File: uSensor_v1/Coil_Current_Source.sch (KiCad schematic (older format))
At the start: 12 parts

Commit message: Schematic in progress.
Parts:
- gave numbers to parts that had none: 12
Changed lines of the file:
@@
 P 5250 3700
 AR Path="/5C48099D" Ref="U?"  Part="1"
-AR Path="/5C398D6C/5C48099D" Ref="U?"  Part="1"
-AR Path="/5C839FF6/5C48099D" Ref="U?"  Part="1"
-F 0 "U?" H 5350 3800 50  0000 L CNN
+AR Path="/5C398D6C/5C48099D" Ref="U17"  Part="1"
+AR Path="/5C839FF6/5C48099D" Ref="U18"  Part="1"
+F 0 "U18" H 5350 3800 50  0000 L CNN
 F 1 "LM6132A/NS" H 5500 3800 50  0000 L CNN
 F 2 "" H 5250 3700 50  0001 C CNN
@@
 P 5500 3000
 AR Path="/5C4809A6" Ref="C?"  Part="1"
-AR Path="/5C398D6C/5C4809A6" Ref="C?"  Part="1"
-AR Path="/5C839FF6/5C4809A6" Ref="C?"  Part="1"
-F 0 "C?" H 5615 3046 50  0000 L CNN
+AR Path="/5C398D6C/5C4809A6" Ref="C54"  Part="1"
+AR Path="/5C839FF6/5C4809A6" Ref="C56"  Part="1"
+F 0 "C56" H 5615 3046 50  0000 L CNN
 F 1 "100n 6V3 X5R" H 5615 2955 50  0000 L CNN
 F 2 "Capacitor_SMD:C_0603_1608Metric_Pad1.05x0.95mm_HandSolder" H 5538 2850 50  0001 C CNN
@@
 P 5500 4600
 AR Path="/5C4809BF" Ref="C?"  Part="1"
-AR Path="/5C398D6C/5C4809BF" Ref="C?"  Part="1"
-AR Path="/5C839FF6/5C4809BF" Ref="C?"  Part="1"
-F 0 "C?" H 5615 4646 50  0000 L CNN
+AR Path="/5C398D6C/5C4809BF" Ref="C55"  Part="1"
+AR Path="/5C839FF6/5C4809BF" Ref="C57"  Part="1"
+F 0 "C57" H 5615 4646 50  0000 L CNN
 F 1 "100n 6V3 X5R" H 5615 4555 50  0000 L CNN
 F 2 "Capacitor_SMD:C_0603_1608Metric_Pad1.05x0.95mm_HandSolder" H 5538 4450 50  0001 C CNN
@@
 P 3900 4050
 AR Path="/5C4809DE" Ref="R?"  Part="1"
-AR Path="/5C398D6C/5C4809DE" Ref="R?"  Part="1"
-AR Path="/5C839FF6/5C4809DE" Ref="R?"  Part="1"
-F 0 "R?" H 3970 4096 50  0000 L CNN
+AR Path="/5C398D6C/5C4809DE" Ref="R42"  Part="1"
+AR Path="/5C839FF6/5C4809DE" Ref="R49"  Part="1"
+F 0 "R49" H 3970 4096 50  0000 L CNN
 F 1 "10k 1%" H 3970 4005 50  0000 L CNN
 F 2 "Resistor_SMD:R_0603_1608Metric_Pad1.05x0.95mm_HandSolder" V 3830 4050 50  0001 C CNN
@@
 P 3900 3550
 AR Path="/5C4809E6" Ref="R?"  Part="1"
-AR Path="/5C398D6C/5C4809E6" Ref="R?"  Part="1"
-AR Path="/5C839FF6/5C4809E6" Ref="R?"  Part="1"
-F 0 "R?" H 3970 3596 50  0000 L CNN
+AR Path="/5C398D6C/5C4809E6" Ref="R40"  Part="1"
+AR Path="/5C839FF6/5C4809E6" Ref="R47"  Part="1"
+F 0 "R47" H 3970 3596 50  0000 L CNN
 F 1 "10k 1%" H 3970 3505 50  0000 L CNN
 F 2 "Resistor_SMD:R_0603_1608Metric_Pad1.05x0.95mm_HandSolder" V 3830 3550 50  0001 C CNN
@@
 P 3450 3550
 AR Path="/5C4809ED" Ref="R?"  Part="1"
-AR Path="/5C398D6C/5C4809ED" Ref="R?"  Part="1"
-AR Path="/5C839FF6/5C4809ED" Ref="R?"  Part="1"
-F 0 "R?" H 3520 3596 50  0000 L CNN
+AR Path="/5C398D6C/5C4809ED" Ref="R39"  Part="1"
+AR Path="/5C839FF6/5C4809ED" Ref="R46"  Part="1"
+F 0 "R46" H 3520 3596 50  0000 L CNN
 F 1 "10k 1%" H 3520 3505 50  0000 L CNN
 F 2 "Resistor_SMD:R_0603_1608Metric_Pad1.05x0.95mm_HandSolder" V 3380 3550 50  0001 C CNN
@@
 P 6700 3400
 AR Path="/5C4809FD" Ref="Q?"  Part="1"
-AR Path="/5C398D6C/5C4809FD" Ref="Q?"  Part="1"
-AR Path="/5C839FF6/5C4809FD" Ref="Q?"  Part="1"
-F 0 "Q?" H 6891 3446 50  0000 L CNN
+AR Path="/5C398D6C/5C4809FD" Ref="Q3"  Part="1"
+AR Path="/5C839FF6/5C4809FD" Ref="Q5"  Part="1"
+F 0 "Q5" H 6891 3446 50  0000 L CNN
 F 1 "Q_NPN_BCE" H 6891 3355 50  0000 L CNN
 F 2 "" H 6900 3500 50  0001 C CNN
@@
 P 6700 4000
 AR Path="/5C480A04" Ref="Q?"  Part="1"
-AR Path="/5C398D6C/5C480A04" Ref="Q?"  Part="1"
-AR Path="/5C839FF6/5C480A04" Ref="Q?"  Part="1"
-F 0 "Q?" H 6891 3954 50  0000 L CNN
+AR Path="/5C398D6C/5C480A04" Ref="Q4"  Part="1"
+AR Path="/5C839FF6/5C480A04" Ref="Q6"  Part="1"
+F 0 "Q6" H 6891 3954 50  0000 L CNN
 F 1 "Q_PNP_BCE" H 6891 4045 50  0000 L CNN
 F 2 "" H 6900 4100 50  0001 C CNN
@@
 P 6550 3700
 AR Path="/5C480A0B" Ref="R?"  Part="1"
-AR Path="/5C398D6C/5C480A0B" Ref="R?"  Part="1"
-AR Path="/5C839FF6/5C480A0B" Ref="R?"  Part="1"
-F 0 "R?" V 6450 3700 50  0000 C CNN
+AR Path="/5C398D6C/5C480A0B" Ref="R41"  Part="1"
+AR Path="/5C839FF6/5C480A0B" Ref="R48"  Part="1"
+F 0 "R48" V 6450 3700 50  0000 C CNN
 F 1 "10k" V 6650 3700 50  0000 C CNN
 F 2 "Resistor_SMD:R_0603_1608Metric_Pad1.05x0.95mm_HandSolder" V 6480 3700 50  0001 C CNN
@@
 P 6800 2950
 AR Path="/5C480A1D" Ref="R?"  Part="1"
-AR Path="/5C398D6C/5C480A1D" Ref="R?"  Part="1"
-AR Path="/5C839FF6/5C480A1D" Ref="R?"  Part="1"
-F 0 "R?" H 6870 2996 50  0000 L CNN
+AR Path="/5C398D6C/5C480A1D" Ref="R38"  Part="1"
+AR Path="/5C839FF6/5C480A1D" Ref="R45"  Part="1"
+F 0 "R45" H 6870 2996 50  0000 L CNN
 F 1 "1R" H 6870 2905 50  0000 L CNN
 F 2 "Resistor_SMD:R_0603_1608Metric_Pad1.05x0.95mm_HandSolder" V 6730 2950 50  0001 C CNN
@@
 P 6800 4450
 AR Path="/5C480A25" Ref="R?"  Part="1"
-AR Path="/5C398D6C/5C480A25" Ref="R?"  Part="1"
-AR Path="/5C839FF6/5C480A25" Ref="R?"  Part="1"
-F 0 "R?" H 6870 4496 50  0000 L CNN
+AR Path="/5C398D6C/5C480A25" Ref="R44"  Part="1"
+AR Path="/5C839FF6/5C480A25" Ref="R51"  Part="1"
+F 0 "R51" H 6870 4496 50  0000 L CNN
 F 1 "1R" H 6870 4405 50  0000 L CNN
 F 2 "Resistor_SMD:R_0603_1608Metric_Pad1.05x0.95mm_HandSolder" V 6730 4450 50  0001 C CNN
@@
 P 8200 4250
 AR Path="/5C480A49" Ref="R?"  Part="1"
-AR Path="/5C398D6C/5C480A49" Ref="R?"  Part="1"
-AR Path="/5C839FF6/5C480A49" Ref="R?"  Part="1"
-F 0 "R?" V 8100 4250 50  0000 C CNN
+AR Path="/5C398D6C/5C480A49" Ref="R43"  Part="1"
+AR Path="/5C839FF6/5C480A49" Ref="R50"  Part="1"
+F 0 "R50" V 8100 4250 50  0000 C CNN
 F 1 "10R" V 8300 4250 50  0000 C CNN
 F 2 "Resistor_SMD:R_0603_1608Metric_Pad1.05x0.95mm_HandSolder" V 8130 4250 50  0001 C CNN

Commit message: Schematic in progress.
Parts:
- Q3, Q4: footprint (none) -> TBD
- U17: value LM6132A/NS -> TBD LM6132A/NS
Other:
- note added: "?"
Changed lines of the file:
@@
 $Descr A4 11693 8268
 encoding utf-8
-Sheet 4 7
+Sheet 3 7
 Title ""
 Date ""
@@
 AR Path="/5C398D6C/5C48099D" Ref="U17"  Part="1"
 AR Path="/5C839FF6/5C48099D" Ref="U18"  Part="1"
-F 0 "U18" H 5350 3800 50  0000 L CNN
-F 1 "LM6132A/NS" H 5500 3800 50  0000 L CNN
+F 0 "U17" H 5350 3800 50  0000 L CNN
+F 1 "TBD LM6132A/NS" H 5350 3550 50  0000 L CNN
 F 2 "" H 5250 3700 50  0001 C CNN
 F 3 "http://www.analog.com/media/en/technical-documentation/data-sheets/AD8603_8607_8609.pdf" H 5250 3900 50  0001 C CNN
@@
 AR Path="/5C398D6C/5C4809A6" Ref="C54"  Part="1"
 AR Path="/5C839FF6/5C4809A6" Ref="C56"  Part="1"
-F 0 "C56" H 5615 3046 50  0000 L CNN
+F 0 "C54" H 5615 3046 50  0000 L CNN
 F 1 "100n 6V3 X5R" H 5615 2955 50  0000 L CNN
 F 2 "Capacitor_SMD:C_0603_1608Metric_Pad1.05x0.95mm_HandSolder" H 5538 2850 50  0001 C CNN
@@
 AR Path="/5C398D6C/5C4809BF" Ref="C55"  Part="1"
 AR Path="/5C839FF6/5C4809BF" Ref="C57"  Part="1"
-F 0 "C57" H 5615 4646 50  0000 L CNN
+F 0 "C55" H 5615 4646 50  0000 L CNN
 F 1 "100n 6V3 X5R" H 5615 4555 50  0000 L CNN
 F 2 "Capacitor_SMD:C_0603_1608Metric_Pad1.05x0.95mm_HandSolder" H 5538 4450 50  0001 C CNN
@@
 AR Path="/5C398D6C/5C4809DE" Ref="R42"  Part="1"
 AR Path="/5C839FF6/5C4809DE" Ref="R49"  Part="1"
-F 0 "R49" H 3970 4096 50  0000 L CNN
+F 0 "R42" H 3970 4096 50  0000 L CNN
 F 1 "10k 1%" H 3970 4005 50  0000 L CNN
 F 2 "Resistor_SMD:R_0603_1608Metric_Pad1.05x0.95mm_HandSolder" V 3830 4050 50  0001 C CNN
@@
 AR Path="/5C398D6C/5C4809E6" Ref="R40"  Part="1"
 AR Path="/5C839FF6/5C4809E6" Ref="R47"  Part="1"
-F 0 "R47" H 3970 3596 50  0000 L CNN
+F 0 "R40" H 3970 3596 50  0000 L CNN
 F 1 "10k 1%" H 3970 3505 50  0000 L CNN
 F 2 "Resistor_SMD:R_0603_1608Metric_Pad1.05x0.95mm_HandSolder" V 3830 3550 50  0001 C CNN
@@
 AR Path="/5C398D6C/5C4809ED" Ref="R39"  Part="1"
 AR Path="/5C839FF6/5C4809ED" Ref="R46"  Part="1"
-F 0 "R46" H 3520 3596 50  0000 L CNN
+F 0 "R39" H 3520 3596 50  0000 L CNN
 F 1 "10k 1%" H 3520 3505 50  0000 L CNN
 F 2 "Resistor_SMD:R_0603_1608Metric_Pad1.05x0.95mm_HandSolder" V 3380 3550 50  0001 C CNN
@@
 AR Path="/5C398D6C/5C4809FD" Ref="Q3"  Part="1"
 AR Path="/5C839FF6/5C4809FD" Ref="Q5"  Part="1"
-F 0 "Q5" H 6891 3446 50  0000 L CNN
+F 0 "Q3" H 6891 3446 50  0000 L CNN
 F 1 "Q_NPN_BCE" H 6891 3355 50  0000 L CNN
-F 2 "" H 6900 3500 50  0001 C CNN
+F 2 "TBD" H 6900 3500 50  0001 C CNN
 F 3 "~" H 6700 3400 50  0001 C CNN
 	1    6700 3400
@@
 AR Path="/5C398D6C/5C480A04" Ref="Q4"  Part="1"
 AR Path="/5C839FF6/5C480A04" Ref="Q6"  Part="1"
-F 0 "Q6" H 6891 3954 50  0000 L CNN
+F 0 "Q4" H 6891 3954 50  0000 L CNN
 F 1 "Q_PNP_BCE" H 6891 4045 50  0000 L CNN
-F 2 "" H 6900 4100 50  0001 C CNN
+F 2 "TBD" H 6900 4100 50  0001 C CNN
 F 3 "~" H 6700 4000 50  0001 C CNN
 	1    6700 4000
@@
 AR Path="/5C398D6C/5C480A0B" Ref="R41"  Part="1"
 AR Path="/5C839FF6/5C480A0B" Ref="R48"  Part="1"
-F 0 "R48" V 6450 3700 50  0000 C CNN
+F 0 "R41" V 6450 3700 50  0000 C CNN
 F 1 "10k" V 6650 3700 50  0000 C CNN
 F 2 "Resistor_SMD:R_0603_1608Metric_Pad1.05x0.95mm_HandSolder" V 6480 3700 50  0001 C CNN
@@
 AR Path="/5C398D6C/5C480A1D" Ref="R38"  Part="1"
 AR Path="/5C839FF6/5C480A1D" Ref="R45"  Part="1"
-F 0 "R45" H 6870 2996 50  0000 L CNN
+F 0 "R38" H 6870 2996 50  0000 L CNN
 F 1 "1R" H 6870 2905 50  0000 L CNN
 F 2 "Resistor_SMD:R_0603_1608Metric_Pad1.05x0.95mm_HandSolder" V 6730 2950 50  0001 C CNN
@@
 AR Path="/5C398D6C/5C480A25" Ref="R44"  Part="1"
 AR Path="/5C839FF6/5C480A25" Ref="R51"  Part="1"
-F 0 "R51" H 6870 4496 50  0000 L CNN
+F 0 "R44" H 6870 4496 50  0000 L CNN
 F 1 "1R" H 6870 4405 50  0000 L CNN
 F 2 "Resistor_SMD:R_0603_1608Metric_Pad1.05x0.95mm_HandSolder" V 6730 4450 50  0001 C CNN
@@
 AR Path="/5C398D6C/5C480A49" Ref="R43"  Part="1"
 AR Path="/5C839FF6/5C480A49" Ref="R50"  Part="1"
-F 0 "R50" V 8100 4250 50  0000 C CNN
+F 0 "R43" V 8100 4250 50  0000 C CNN
 F 1 "10R" V 8300 4250 50  0000 C CNN
 F 2 "Resistor_SMD:R_0603_1608Metric_Pad1.05x0.95mm_HandSolder" V 8130 4250 50  0001 C CNN
@@
 Wire Wire Line
 	8200 4400 8200 4500
+Text Notes 5600 3650 0    150  ~ 30
+?
 $EndSCHEMATC

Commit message: Schematic in progress.
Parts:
- U17: value TBD LM6132A/NS -> TBD
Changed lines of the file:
@@
 AR Path="/5C839FF6/5C48099D" Ref="U18"  Part="1"
 F 0 "U17" H 5350 3800 50  0000 L CNN
-F 1 "TBD LM6132A/NS" H 5350 3550 50  0000 L CNN
+F 1 "TBD" H 5350 3550 50  0000 L CNN
 F 2 "" H 5250 3700 50  0001 C CNN
 F 3 "http://www.analog.com/media/en/technical-documentation/data-sheets/AD8603_8607_8609.pdf" H 5250 3900 50  0001 C CNN

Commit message: Schematic in progress.
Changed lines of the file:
@@
 $Descr A4 11693 8268
 encoding utf-8
-Sheet 3 7
+Sheet 4 7
 Title ""
 Date ""
@@
 AR Path="/5C398D6C/5C48099D" Ref="U17"  Part="1"
 AR Path="/5C839FF6/5C48099D" Ref="U18"  Part="1"
-F 0 "U17" H 5350 3800 50  0000 L CNN
+F 0 "U18" H 5350 3800 50  0000 L CNN
 F 1 "TBD" H 5350 3550 50  0000 L CNN
 F 2 "" H 5250 3700 50  0001 C CNN
@@
 AR Path="/5C398D6C/5C4809A6" Ref="C54"  Part="1"
 AR Path="/5C839FF6/5C4809A6" Ref="C56"  Part="1"
-F 0 "C54" H 5615 3046 50  0000 L CNN
+F 0 "C56" H 5615 3046 50  0000 L CNN
 F 1 "100n 6V3 X5R" H 5615 2955 50  0000 L CNN
 F 2 "Capacitor_SMD:C_0603_1608Metric_Pad1.05x0.95mm_HandSolder" H 5538 2850 50  0001 C CNN
@@
 AR Path="/5C398D6C/5C4809BF" Ref="C55"  Part="1"
 AR Path="/5C839FF6/5C4809BF" Ref="C57"  Part="1"
-F 0 "C55" H 5615 4646 50  0000 L CNN
+F 0 "C57" H 5615 4646 50  0000 L CNN
 F 1 "100n 6V3 X5R" H 5615 4555 50  0000 L CNN
 F 2 "Capacitor_SMD:C_0603_1608Metric_Pad1.05x0.95mm_HandSolder" H 5538 4450 50  0001 C CNN
@@
 AR Path="/5C398D6C/5C4809DE" Ref="R42"  Part="1"
 AR Path="/5C839FF6/5C4809DE" Ref="R49"  Part="1"
-F 0 "R42" H 3970 4096 50  0000 L CNN
+F 0 "R49" H 3970 4096 50  0000 L CNN
 F 1 "10k 1%" H 3970 4005 50  0000 L CNN
 F 2 "Resistor_SMD:R_0603_1608Metric_Pad1.05x0.95mm_HandSolder" V 3830 4050 50  0001 C CNN
@@
 AR Path="/5C398D6C/5C4809E6" Ref="R40"  Part="1"
 AR Path="/5C839FF6/5C4809E6" Ref="R47"  Part="1"
-F 0 "R40" H 3970 3596 50  0000 L CNN
+F 0 "R47" H 3970 3596 50  0000 L CNN
 F 1 "10k 1%" H 3970 3505 50  0000 L CNN
 F 2 "Resistor_SMD:R_0603_1608Metric_Pad1.05x0.95mm_HandSolder" V 3830 3550 50  0001 C CNN
@@
 AR Path="/5C398D6C/5C4809ED" Ref="R39"  Part="1"
 AR Path="/5C839FF6/5C4809ED" Ref="R46"  Part="1"
-F 0 "R39" H 3520 3596 50  0000 L CNN
+F 0 "R46" H 3520 3596 50  0000 L CNN
 F 1 "10k 1%" H 3520 3505 50  0000 L CNN
 F 2 "Resistor_SMD:R_0603_1608Metric_Pad1.05x0.95mm_HandSolder" V 3380 3550 50  0001 C CNN
@@
 AR Path="/5C398D6C/5C4809FD" Ref="Q3"  Part="1"
 AR Path="/5C839FF6/5C4809FD" Ref="Q5"  Part="1"
-F 0 "Q3" H 6891 3446 50  0000 L CNN
+F 0 "Q5" H 6891 3446 50  0000 L CNN
 F 1 "Q_NPN_BCE" H 6891 3355 50  0000 L CNN
 F 2 "TBD" H 6900 3500 50  0001 C CNN
@@
 AR Path="/5C398D6C/5C480A04" Ref="Q4"  Part="1"
 AR Path="/5C839FF6/5C480A04" Ref="Q6"  Part="1"
-F 0 "Q4" H 6891 3954 50  0000 L CNN
+F 0 "Q6" H 6891 3954 50  0000 L CNN
 F 1 "Q_PNP_BCE" H 6891 4045 50  0000 L CNN
 F 2 "TBD" H 6900 4100 50  0001 C CNN
@@
 AR Path="/5C398D6C/5C480A0B" Ref="R41"  Part="1"
 AR Path="/5C839FF6/5C480A0B" Ref="R48"  Part="1"
-F 0 "R41" V 6450 3700 50  0000 C CNN
+F 0 "R48" V 6450 3700 50  0000 C CNN
 F 1 "10k" V 6650 3700 50  0000 C CNN
 F 2 "Resistor_SMD:R_0603_1608Metric_Pad1.05x0.95mm_HandSolder" V 6480 3700 50  0001 C CNN
@@
 AR Path="/5C398D6C/5C480A1D" Ref="R38"  Part="1"
 AR Path="/5C839FF6/5C480A1D" Ref="R45"  Part="1"
-F 0 "R38" H 6870 2996 50  0000 L CNN
+F 0 "R45" H 6870 2996 50  0000 L CNN
 F 1 "1R" H 6870 2905 50  0000 L CNN
 F 2 "Resistor_SMD:R_0603_1608Metric_Pad1.05x0.95mm_HandSolder" V 6730 2950 50  0001 C CNN
@@
 AR Path="/5C398D6C/5C480A25" Ref="R44"  Part="1"
 AR Path="/5C839FF6/5C480A25" Ref="R51"  Part="1"
-F 0 "R44" H 6870 4496 50  0000 L CNN
+F 0 "R51" H 6870 4496 50  0000 L CNN
 F 1 "1R" H 6870 4405 50  0000 L CNN
 F 2 "Resistor_SMD:R_0603_1608Metric_Pad1.05x0.95mm_HandSolder" V 6730 4450 50  0001 C CNN
@@
 AR Path="/5C398D6C/5C480A49" Ref="R43"  Part="1"
 AR Path="/5C839FF6/5C480A49" Ref="R50"  Part="1"
-F 0 "R43" V 8100 4250 50  0000 C CNN
+F 0 "R50" V 8100 4250 50  0000 C CNN
 F 1 "10R" V 8300 4250 50  0000 C CNN
 F 2 "Resistor_SMD:R_0603_1608Metric_Pad1.05x0.95mm_HandSolder" V 8130 4250 50  0001 C CNN
@@
 Text Notes 5600 3650 0    150  ~ 30
 ?
+Text Notes 7400 3450 0    150  ~ 30
+?
+Text Notes 7450 4100 0    150  ~ 30
+?
 $EndSCHEMATC

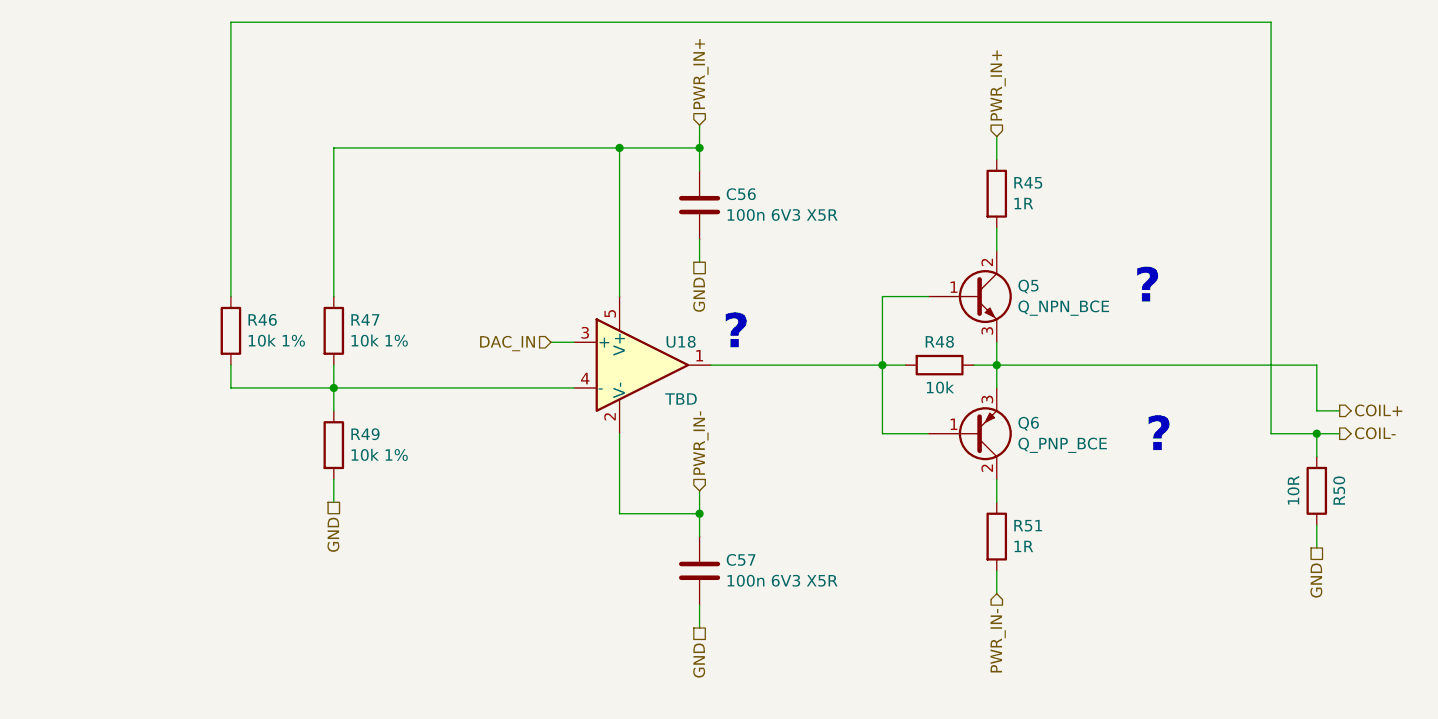
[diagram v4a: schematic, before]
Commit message: Added testpoints to schematic.
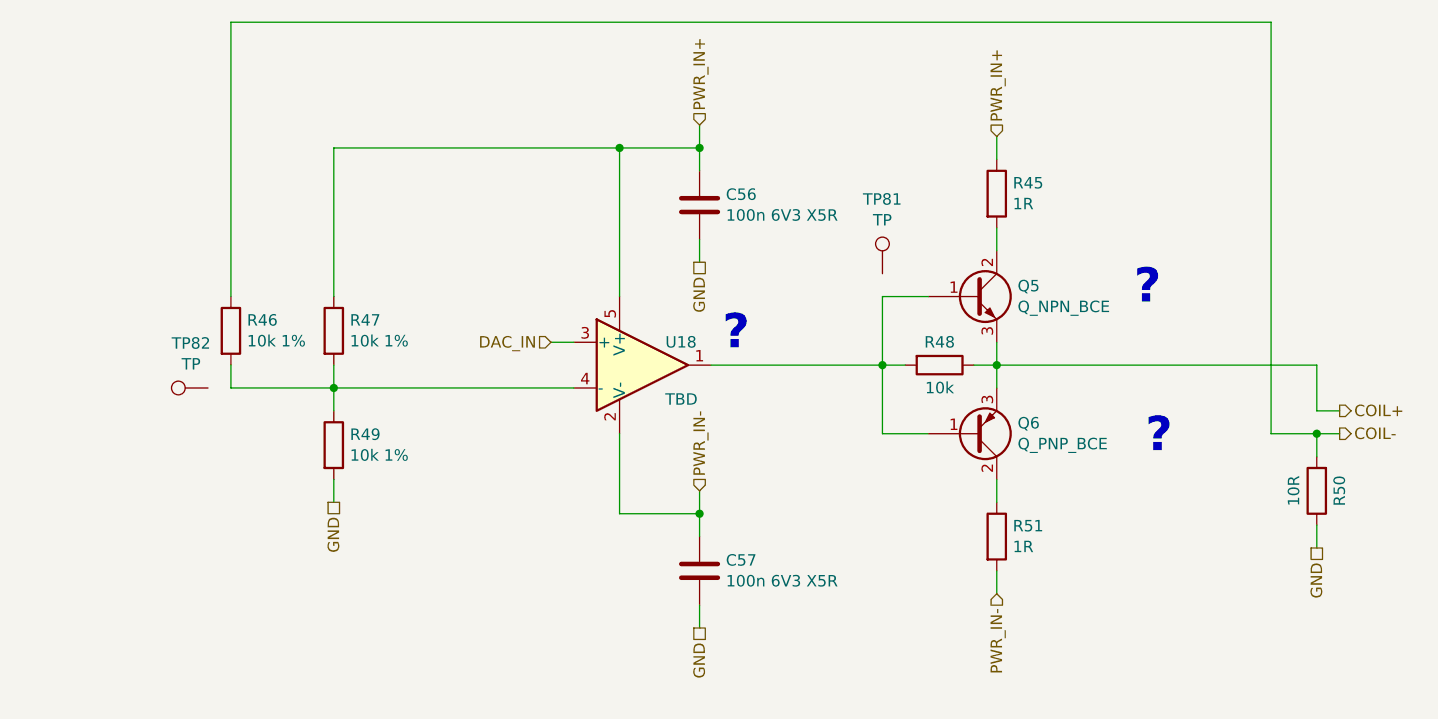
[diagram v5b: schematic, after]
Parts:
- added TP79, TP80: TP, Sentisa-Connectors:TestPoint_Probe_1.0mmDiameter_0.6mmDrill, symbol Connector:TestPoint
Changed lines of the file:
@@
 Text Notes 7450 4100 0    150  ~ 30
 ?
+$Comp
+L Connector:TestPoint TP?
+U 1 1 5D2DDD20
+P 3350 3800
+AR Path="/5D2DDD20" Ref="TP?"  Part="1"
+AR Path="/5C398D6C/5D2DDD20" Ref="TP80"  Part="1"
+AR Path="/5C839FF6/5D2DDD20" Ref="TP82"  Part="1"
+F 0 "TP82" V 3545 3874 50  0000 C CNN
+F 1 "TP" V 3454 3874 50  0000 C CNN
+F 2 "Sentisa-Connectors:TestPoint_Probe_1.0mmDiameter_0.6mmDrill" H 3550 3800 50  0001 C CNN
+F 3 "~" H 3550 3800 50  0001 C CNN
+	1    3350 3800
+	0    -1   -1   0
+$EndComp
+$Comp
+L Connector:TestPoint TP?
+U 1 1 5D2DE6A8
+P 6300 3300
+AR Path="/5D2DE6A8" Ref="TP?"  Part="1"
+AR Path="/5C398D6C/5D2DE6A8" Ref="TP79"  Part="1"
+AR Path="/5C839FF6/5D2DE6A8" Ref="TP81"  Part="1"
+F 0 "TP81" H 6300 3625 50  0000 C CNN
+F 1 "TP" H 6300 3534 50  0000 C CNN
+F 2 "Sentisa-Connectors:TestPoint_Probe_1.0mmDiameter_0.6mmDrill" H 6500 3300 50  0001 C CNN
+F 3 "~" H 6500 3300 50  0001 C CNN
+	1    6300 3300
+	1    0    0    -1
+$EndComp
 $EndSCHEMATC
